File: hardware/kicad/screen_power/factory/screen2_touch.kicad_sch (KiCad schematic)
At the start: 12 parts, among them J201 PI USB, J202 TOUCH, U201 ADuM3165BRSZ, Y201 24MHz 10pF

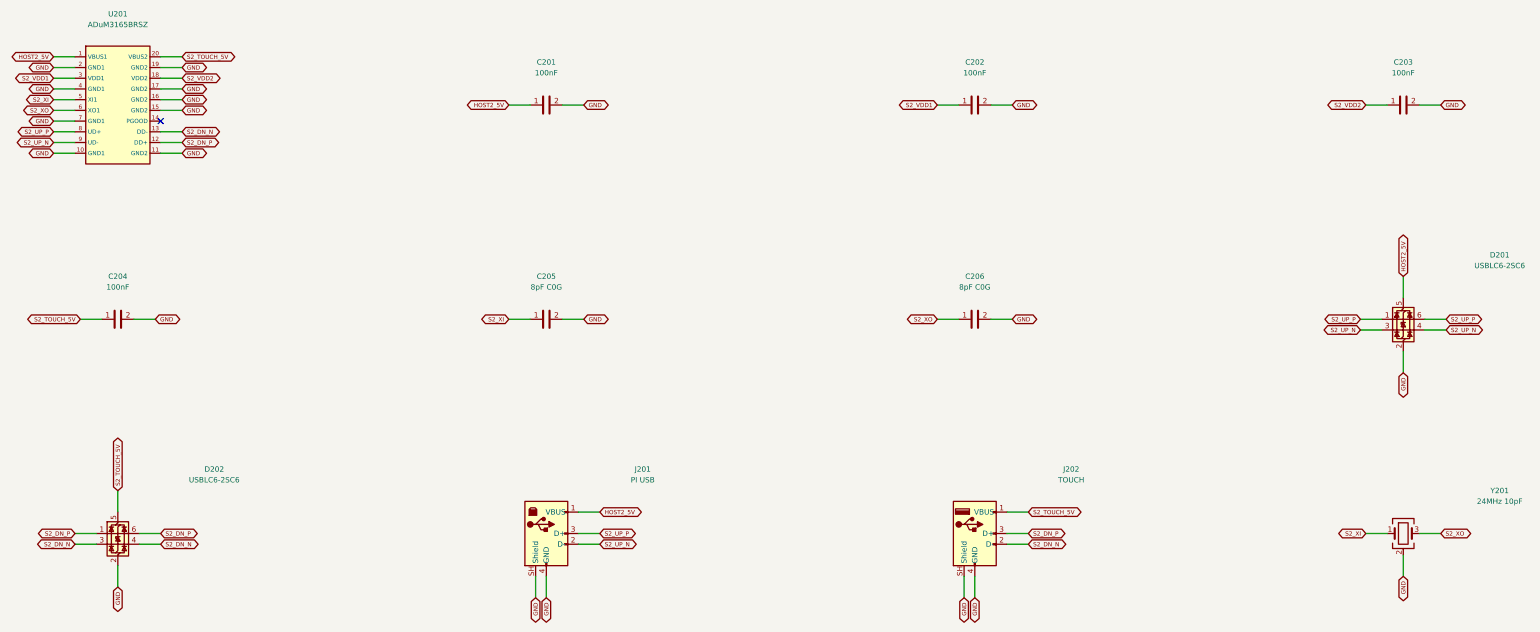
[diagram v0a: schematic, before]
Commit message: refactor(hardware): simplify and compact screen power boards
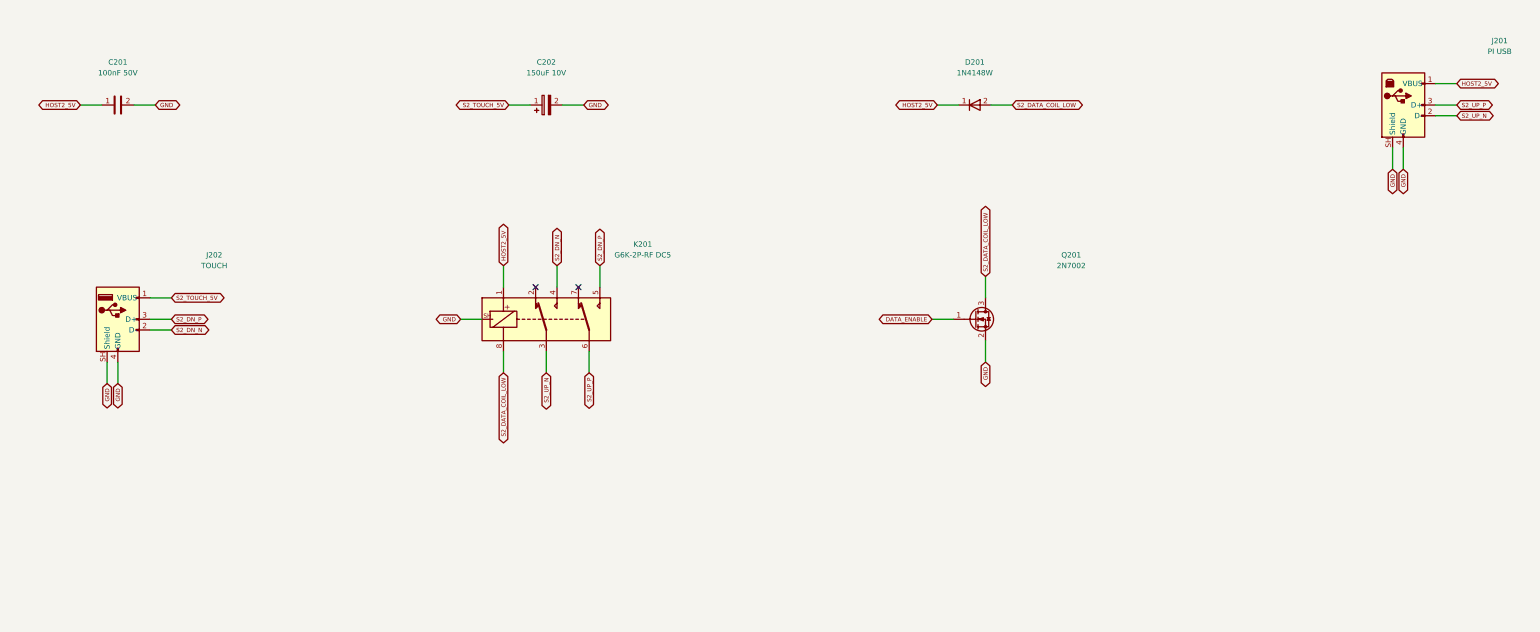
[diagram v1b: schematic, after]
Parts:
- removed C203, C204: 100nF, Capacitor_SMD:C_0805_2012Metric, symbol screen_symbols:Device_C
- removed C205, C206: 8pF C0G, Capacitor_SMD:C_0805_2012Metric, symbol screen_symbols:Device_C
- removed D202: USBLC6-2SC6, Package_TO_SOT_SMD:SOT-23-6, symbol screen_symbols:Power_Protection_USBLC6-2SC6
- removed U201: ADuM3165BRSZ, Package_SO:SSOP-20_5.3x7.2mm_P0.65mm, symbol screen_symbols:screen_power_ADuM3165BRSZ
- removed Y201: 24MHz 10pF, Crystal:Crystal_SMD_3225-4Pin_3.2x2.5mm, symbol screen_symbols:Device_Crystal_GND24
- added K201: G6K-2P-RF DC5, screen_power:Relay_DPDT_Omron_G6K-2P-RF, symbol screen_symbols:screen_power_G6K-2P-RF
- added Q201: 2N7002, Package_TO_SOT_SMD:SOT-23, symbol screen_symbols:Transistor_FET_2N7002
- C201: value 100nF -> 100nF 50V; MPN C0805C104K5RAC -> GRM21BR71H104KA01L
- C202: value 100nF -> 150uF 10V; footprint Capacitor_SMD:C_0805_2012Metric -> Capacitor_THT:CP_Radial_D5.0mm_P2.00mm; symbol screen_symbols:Device_C -> screen_symbols:Device_C_Polarized; MPN C0805C104K5RAC -> EEU-FR1A151
- D201: value USBLC6-2SC6 -> 1N4148W; footprint Package_TO_SOT_SMD:SOT-23-6 -> Diode_SMD:D_SOD-123; symbol screen_symbols:Power_Protection_USBLC6-2SC6 -> screen_symbols:Diode_1N4148W; MPN USBLC6-2SC6 -> 1N4148W-7-F
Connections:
- net S2_VDD1 is gone; now on net S2_TOUCH_5V: C202.1
- net GND: now also K201.SH (CASE), Q201.2 (S); no longer D201.2 (GND)
- net HOST2_5V: now also D201.1 (K), K201.1; no longer D201.5 (VBUS)
- net S2_DN_N: now also K201.4
- net S2_DN_P: now also K201.5
- net S2_UP_N: now also K201.3; no longer D201.3 (I/O2), D201.4 (I/O2)
- net S2_UP_P: now also K201.6; no longer D201.1 (I/O1), D201.6 (I/O1)
- new net DATA_ENABLE: Q201.1 (G)
- new net S2_DATA_COIL_LOW: D201.2 (A), K201.8, Q201.3 (D)
- no-connect marks 1 -> 2
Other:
- moved on the sheet: C201, J201, J202
